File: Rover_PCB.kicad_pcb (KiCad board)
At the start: 2 copper layers, 100 x 100 mm, 73 parts, among them J1 XT90_24V_IN, J19 RJ45, J35 XT90_48V_IN, J38 USB_C_Receptacle_USB2.0_16P, J43 XT90_24V_OUT, J44 XT90_48V_OUT, J45 ATX, J46 Conn_01x30_Socket, J47 FFC, J72 FFC, Q11 AO3400A, Q12 AO3400A, Q13 AO3400A, Q14 AO3400A, Q15 AO3400A, Q16 AO3400A, Q17 AO3400A, Q18 AO3400A, Q5 IRLZ44N, Q6 IRLZ44N, SW1 SW_Push, U1 STM32H743VITx, U10 HX711, U11 HX711, U12 HX711, U2 AMS1117-3.3, U3 LM2596S-5, U4 LM2596S-12, U5 VNH5019A-E, U6 VNH5019A-E, U7 SN65HVD230, U8 SN65HVD230, U9 HX711

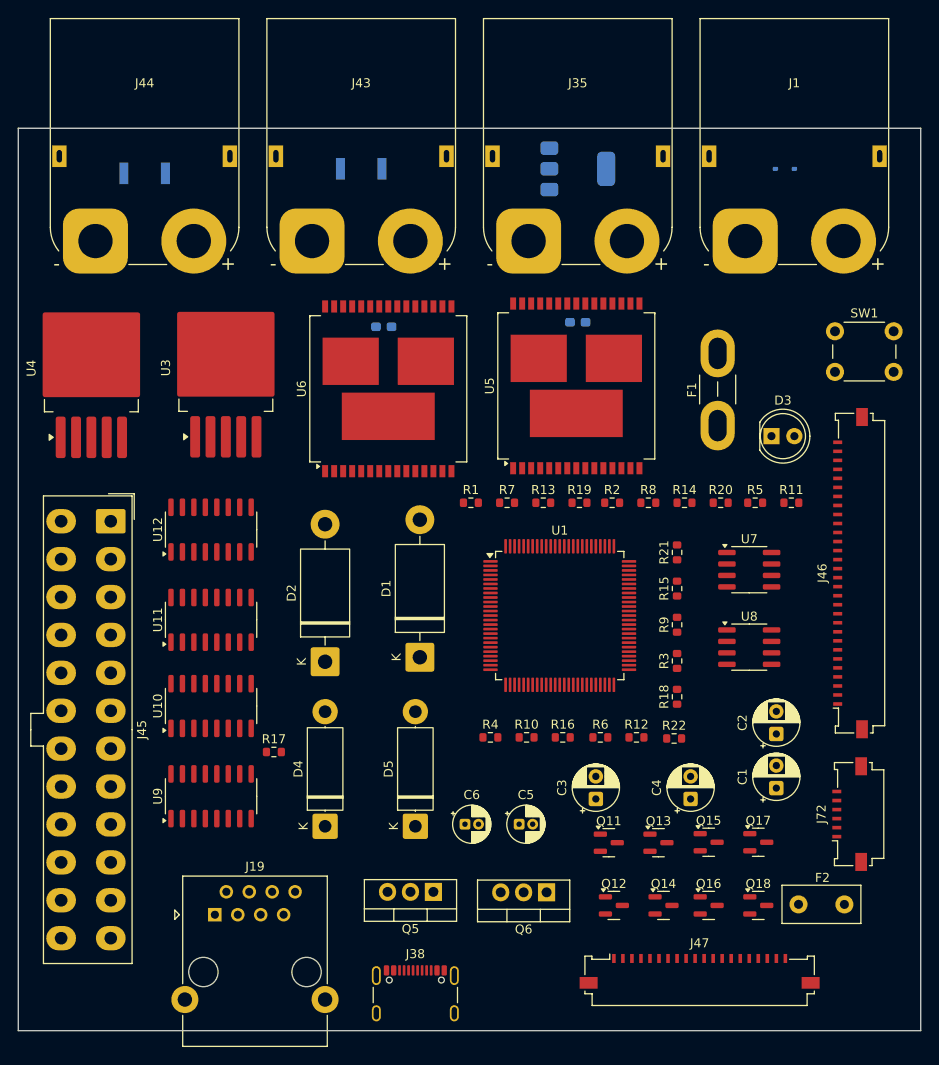
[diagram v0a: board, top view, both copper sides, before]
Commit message: Aktualizacja schematu i PCB: dodanie rezonatora Y2, kondensatorow C9/C10 i punktow testowych J75-J79 oraz aktualizacja README.md i .gitignore
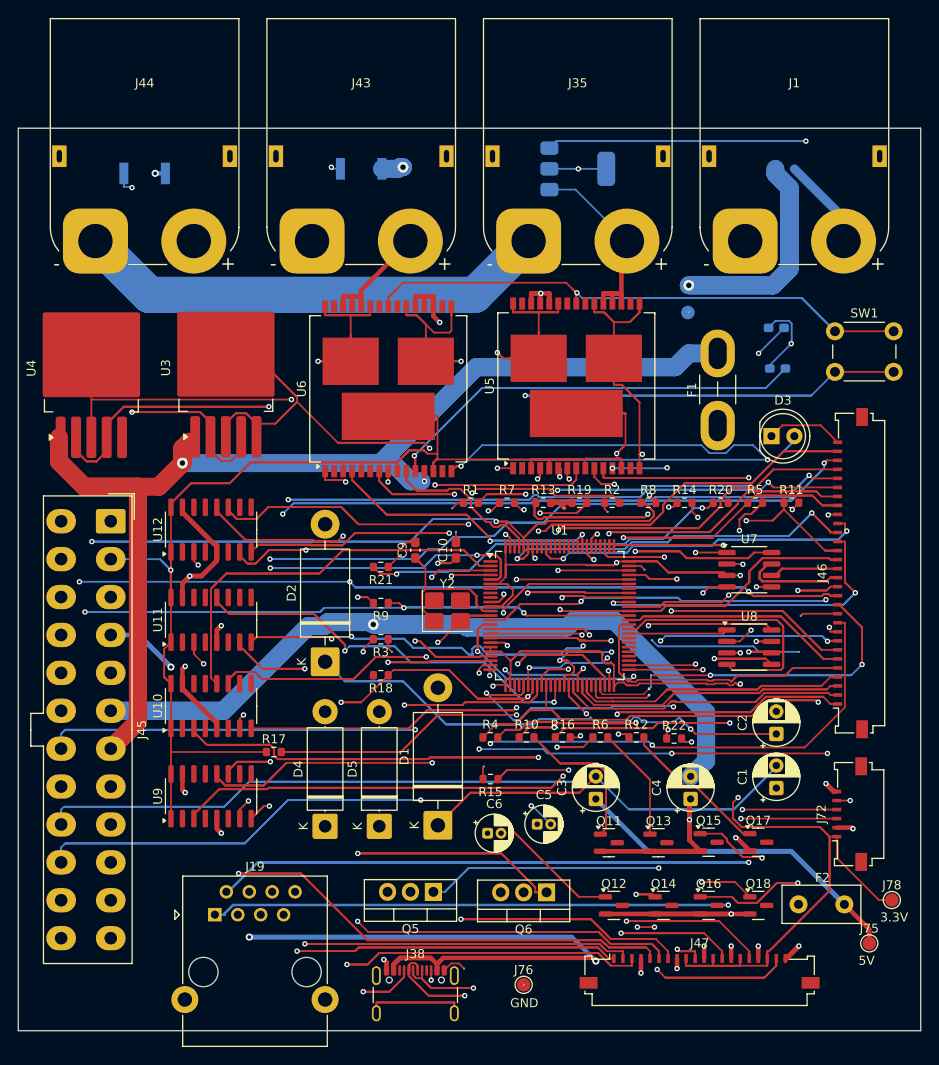
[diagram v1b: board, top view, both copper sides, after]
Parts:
- added C10: 18pF, Capacitor_SMD:C_0603_1608Metric_Pad1.08x0.95mm_HandSolder, F.Cu at (81.0, 95.1)
- added C9: 18pF, Capacitor_SMD:C_0603_1608Metric_Pad1.08x0.95mm_HandSolder, F.Cu at (76.5, 95.1)
- added J75: TEST_PAD 5V, TestPoint:TestPoint_Pad_D1.5mm, F.Cu at (126.8, 138.7)
- added J76: TEST_PAD GND, TestPoint:TestPoint_Pad_D1.5mm, F.Cu at (88.5, 143.3)
- added J77: TEST_PAD 24V, TestPoint:TestPoint_Pad_D1.5mm, B.Cu at (106.7, 68.8)
- added J78: TEST_PAD 3.3V, TestPoint:TestPoint_Pad_D1.5mm, F.Cu at (129.3, 133.9)
- added J79: TEST_PAD 12V, TestPoint:TestPoint_Pad_D1.5mm, B.Cu at (55.5, 112.6)
- added Y2: 8MHz, Crystal:Crystal_SMD_3225-4Pin_3.2x2.5mm_HandSoldering, F.Cu at (80.0, 101.8)
- moved C7 43.5 mm to (116.5, 70.5)
- moved R3 32.9 mm to (72.7, 105.0), turned to 180 degrees
- moved R9 32.9 mm to (72.7, 101.0), turned to 180 degrees
- moved R18 32.9 mm to (72.7, 109.0), turned to 180 degrees
- moved R21 32.9 mm to (72.7, 97.0), turned to 180 degrees
- moved R15 29.5 mm to (84.8, 120.5), turned to 180 degrees
- moved C8 22.7 mm to (116.6, 75.0)
- moved D1 18.7 mm to (79.0, 125.6)
- moved D5 4.00 mm to (72.5, 125.7)
- moved C6 2.69 mm to (84.5, 126.5)
- moved C5 2.00 mm to (90.0, 125.5)
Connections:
- J19 pad 1: /OUTA2 -> /CANH_ETH
- J19 pad 2: /OUTB2 -> /CANL_ETH
- U1 pad 12: unconnected-(U1-PH0-Pad12) -> Net-(U1-PH0)
- U1 pad 13: unconnected-(U1-PH1-Pad13) -> Net-(U1-PH1)
- U1 pad 24: unconnected-(U1-PA2-Pad24) -> /TX1
- U1 pad 25: unconnected-(U1-PA3-Pad25) -> /RX1
- U1 pad 46: unconnected-(U1-PB10-Pad46) -> /TX2
- U1 pad 47: unconnected-(U1-PB11-Pad47) -> /RX2
- U12 pad 11: /Pe12 -> /PE12
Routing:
- net /+3.3V: track 0.00 -> 621.2 mm, vias 0 -> 9
- net /+24V: track 0.00 -> 396.2 mm, vias 0 -> 6
- net /+5V: track 0.00 -> 364.6 mm, vias 0 -> 4
- net /OUTB2: track 0.00 -> 282.3 mm, vias 0 -> 5
- net /+12V: track 0.00 -> 275.1 mm, vias 0 -> 2
- net /+48V: track 0.00 -> 261.2 mm
- net /GND: track 0.00 -> 253.6 mm, vias 0 -> 41
- net /OUTA2: track 0.00 -> 250.3 mm, vias 0 -> 5
- net /OUTB1: track 0.00 -> 239.8 mm, vias 0 -> 2
- net Net-(D1-K): track 0.00 -> 237.6 mm, vias 0 -> 1
- net /PB9: track 0.00 -> 223.3 mm, vias 0 -> 2
- net /OUTA1: track 0.00 -> 213.1 mm, vias 0 -> 3
- net Net-(U2-VI): track 0.00 -> 191.1 mm, vias 0 -> 1
- net /AVDD: track 0.00 -> 188.8 mm, vias 0 -> 2
- net /AVDD1: track 0.00 -> 187.4 mm, vias 0 -> 2
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- added copper zone on In2.Cu, net /GND
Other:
- copper layers 2 -> 4
- board text added: "3.3V"
- board text added: "5V"
- board text added: "GND"

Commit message: Aktualizacja plytki zasilania (Power), uaktualnienie README.md o szczegoly klas netow i grubosci sciezek na obu plytkach
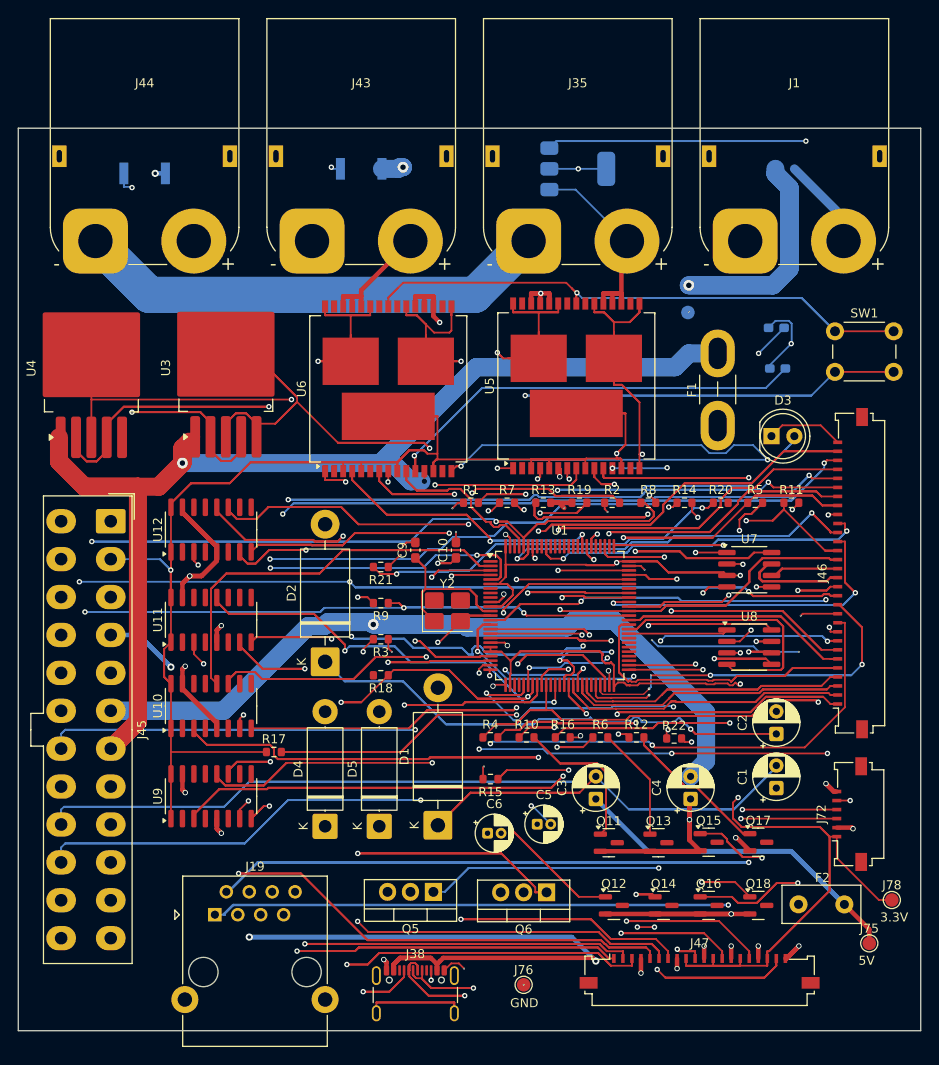
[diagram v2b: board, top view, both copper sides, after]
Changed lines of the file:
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@@
 		(at 51 108)
 		(size 0.6)
-		(drill 0.3)
+		(drill 0.4)
 		(layers "F.Cu" "B.Cu")
 		(net 1)
@@
 		(at 85.1 110.2)
 		(size 0.6)
-		(drill 0.3)
+		(drill 0.4)
 		(layers "F.Cu" "B.Cu")
 		(net 1)
@@
 		(at 86.5 93.4)
 		(size 0.6)
-		(drill 0.3)
+		(drill 0.4)
 		(layers "F.Cu" "B.Cu")
 		(net 1)
@@
 		(at 86.7 105.7)
 		(size 0.6)
-		(drill 0.3)
+		(drill 0.4)
 		(layers "F.Cu" "B.Cu")
 		(net 1)
@@
 		(at 105.5 141.5)
 		(size 0.6)
-		(drill 0.3)
+		(drill 0.4)
 		(layers "F.Cu" "B.Cu")
 		(net 1)
@@
 		(at 114.5 139)
 		(size 0.6)
-		(drill 0.3)
+		(drill 0.4)
 		(layers "F.Cu" "B.Cu")
 		(net 1)
@@
 		(at 55 103.5)
 		(size 0.6)
-		(drill 0.3)
+		(drill 0.4)
 		(layers "F.Cu" "B.Cu")
 		(net 1)
@@
 		(at 112 127)
 		(size 0.6)
-		(drill 0.3)
+		(drill 0.4)
 		(layers "F.Cu" "B.Cu")
 		(net 1)
@@
 		(at 119 139)
 		(size 0.6)
-		(drill 0.3)
+		(drill 0.4)
 		(layers "F.Cu" "B.Cu")
 		(net 1)
@@
 		(at 108.5 139)
 		(size 0.6)
-		(drill 0.3)
+		(drill 0.4)
 		(layers "F.Cu" "B.Cu")
 		(net 1)
@@
 		(at 86.3 100)
 		(size 0.6)
-		(drill 0.3)
+		(drill 0.4)
 		(layers "F.Cu" "B.Cu")
 		(net 1)
@@
 		(at 55 126.5)
 		(size 0.6)
-		(drill 0.3)
+		(drill 0.4)
 		(layers "F.Cu" "B.Cu")
 		(net 1)
@@
 		(at 125 126)
 		(size 0.6)
-		(drill 0.3)
+		(drill 0.4)
 		(layers "F.Cu" "In2.Cu")
 		(net 1)
@@
 		(at 101.5 142)
 		(size 0.6)
-		(drill 0.3)
+		(drill 0.4)
 		(layers "F.Cu" "B.Cu")
 		(net 1)
@@
 		(at 106.874 125)
 		(size 0.6)
-		(drill 0.3)
+		(drill 0.4)
 		(layers "F.Cu" "B.Cu")
 		(net 1)
@@
 		(at 97.9 108.5)
 		(size 0.6)
-		(drill 0.3)
+		(drill 0.4)
 		(layers "F.Cu" "B.Cu")
 		(net 1)
@@
 		(at 73 140.5)
 		(size 0.6)
-		(drill 0.3)
+		(drill 0.4)
 		(layers "F.Cu" "B.Cu")
 		(net 1)
@@
 		(at 51.5 98)
 		(size 0.6)
-		(drill 0.3)
+		(drill 0.4)
 		(layers "F.Cu" "B.Cu")
 		(net 1)
@@
 		(at 51 122)
 		(size 0.6)
-		(drill 0.3)
+		(drill 0.4)
 		(layers "F.Cu" "B.Cu")
 		(net 1)
@@
 		(at 122 121)
 		(size 0.6)
-		(drill 0.3)
+		(drill 0.4)
 		(layers "F.Cu" "In2.Cu")
 		(net 1)
@@
 		(at 92.5 87)
 		(size 0.6)
-		(drill 0.3)
+		(drill 0.4)
 		(layers "F.Cu" "B.Cu")
 		(net 1)
@@
 		(at 94.8 115.7)
 		(size 0.6)
-		(drill 0.3)
+		(drill 0.4)
 		(layers "F.Cu" "B.Cu")
 		(net 1)
@@
 		(at 111.5 135.45)
 		(size 0.6)
-		(drill 0.3)
+		(drill 0.4)
 		(layers "F.Cu" "B.Cu")
 		(net 1)
@@
 		(at 111.5 139)
 		(size 0.6)
-		(drill 0.3)
+		(drill 0.4)
 		(layers "F.Cu" "B.Cu")
 		(net 1)
@@
 		(at 77.5 87.5)
 		(size 0.6)
-		(drill 0.3)
+		(drill 0.6)
 		(layers "F.Cu" "B.Cu")
 		(net 37)
